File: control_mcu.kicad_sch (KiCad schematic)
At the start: 23 parts, among them J401 Conn_02x02_Top_Bottom, J402 Conn_02x06_Odd_Even, U401 ATtiny1616-MNR

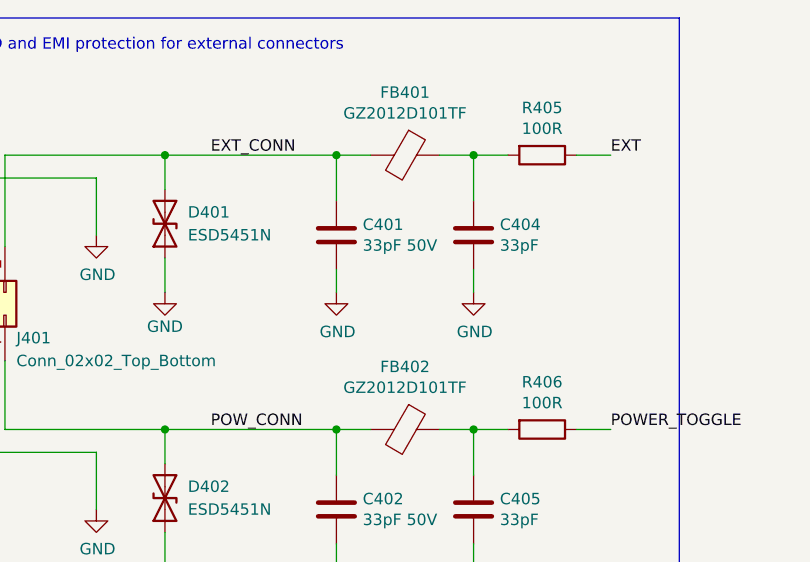
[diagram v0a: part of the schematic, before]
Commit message: Correct part LCSC codes and values
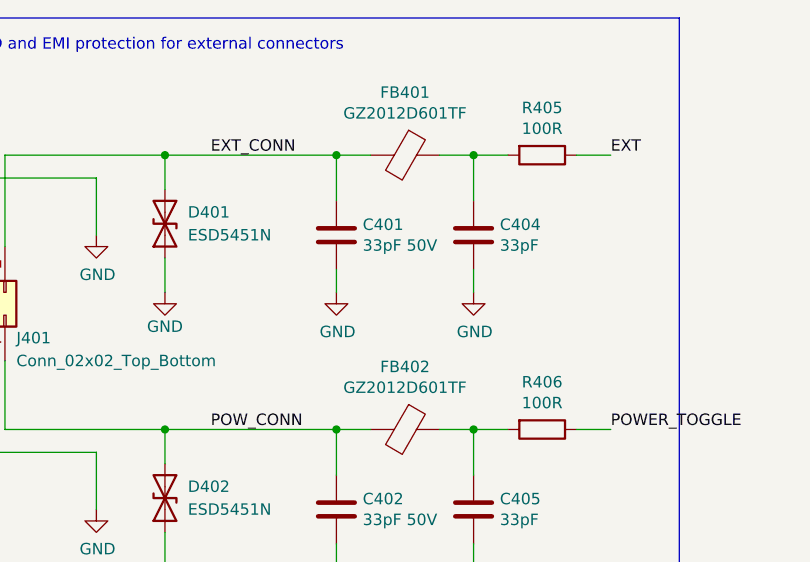
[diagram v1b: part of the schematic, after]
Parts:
- FB401, FB402: value GZ2012D101TF -> GZ2012D601TF
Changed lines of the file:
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@@
     (in_bom yes) (on_board yes)
     (property "Reference" "FB401" (id 0) (at 66.04 23.5204 90))
-    (property "Value" "GZ2012D101TF" (id 1) (at 66.04 25.8318 90))
+    (property "Value" "GZ2012D601TF" (id 1) (at 66.04 25.8318 90))
     (property "Footprint" "Inductor_SMD:L_0805_2012Metric" (id 2) (at 66.04 28.702 90)
       (effects (font (size 1.27 1.27)) hide)
@@
     (in_bom yes) (on_board yes)
     (property "Reference" "FB402" (id 0) (at 66.04 54.0004 90))
-    (property "Value" "GZ2012D101TF" (id 1) (at 66.04 56.3118 90))
+    (property "Value" "GZ2012D601TF" (id 1) (at 66.04 56.3118 90))
     (property "Footprint" "Inductor_SMD:L_0805_2012Metric" (id 2) (at 66.04 59.182 90)
       (effects (font (size 1.27 1.27)) hide)

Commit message: Move rotation definitions to component fields
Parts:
- J401: JLCPCB_CORRECTION (none) -> 1.27;1.27;90
- J402: JLCPCB_CORRECTION (none) -> 1.27;6.35;90
- U401: JLCPCB_CORRECTION (none) -> 0;0;270

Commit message: Replace parts due to lack of availability
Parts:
- J402: LCSC C492423 -> C5383107
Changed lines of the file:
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@@
 			)
 		)
-		(property "LCSC" "C492423"
+		(property "LCSC" "C5383107"
 			(at 243.84 74.93 0)
 			(effects
